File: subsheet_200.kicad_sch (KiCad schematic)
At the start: 24 parts, among them J200 DIN-5S — MIDI OUT/THRU, J201 DIN-5S — MIDI IN, U200 MC6850_PHY, U208 PC900_PHY, U210 7406_PHY

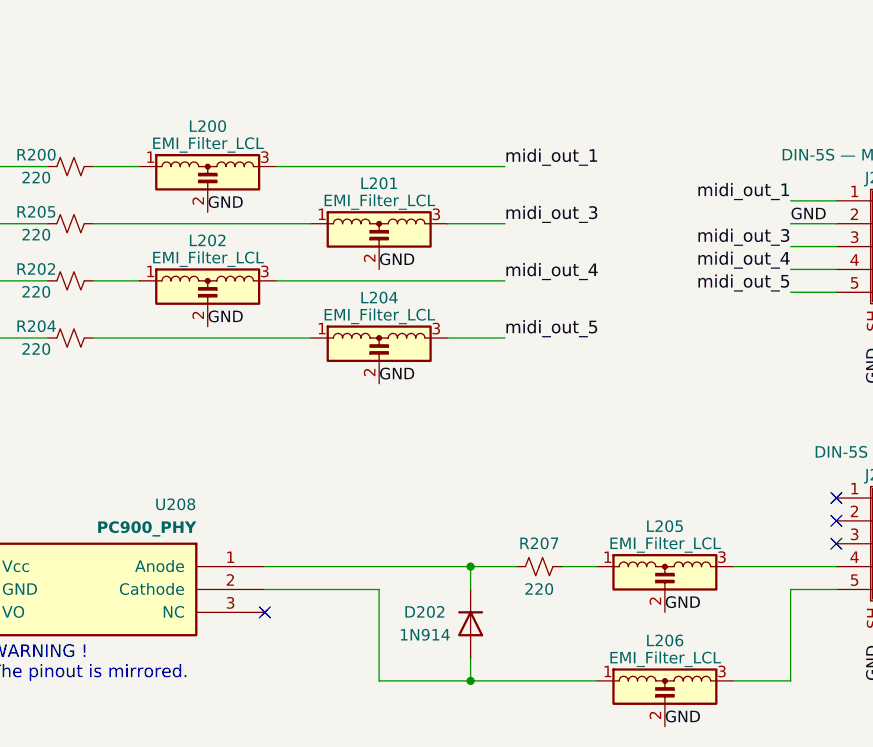
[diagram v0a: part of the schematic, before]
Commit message: Resolves #3 : [schematic] annotate video port with signal name
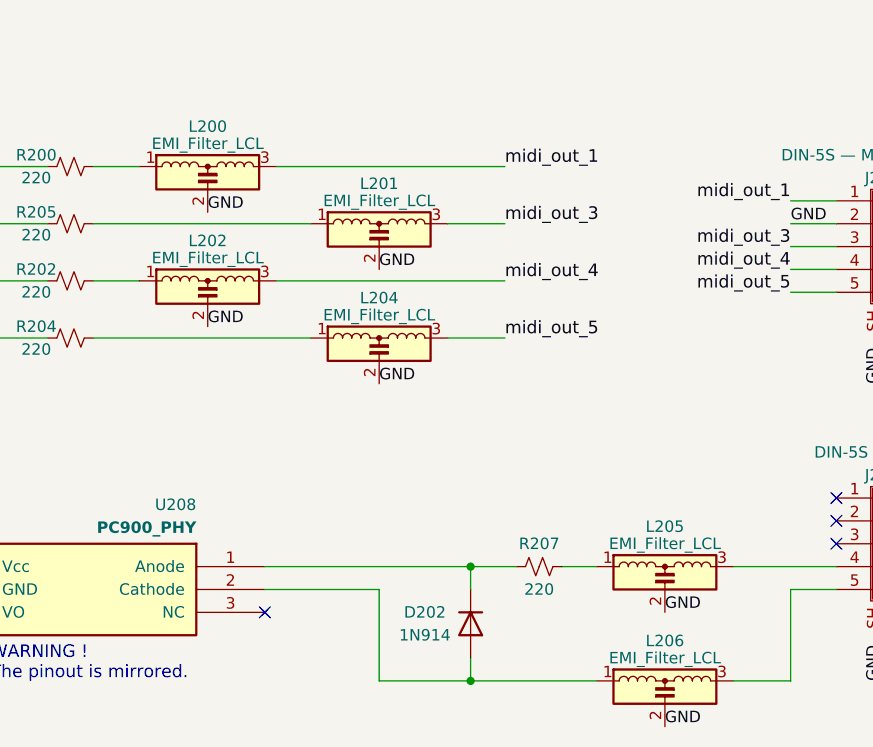
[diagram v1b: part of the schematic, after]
